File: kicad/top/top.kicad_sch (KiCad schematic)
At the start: 32 parts, among them J1 OLED_128x32, J2 Conn_01x15, SW1 SLW-864574-5A-RA-N-D, SW2 RotaryEncoder_Switch

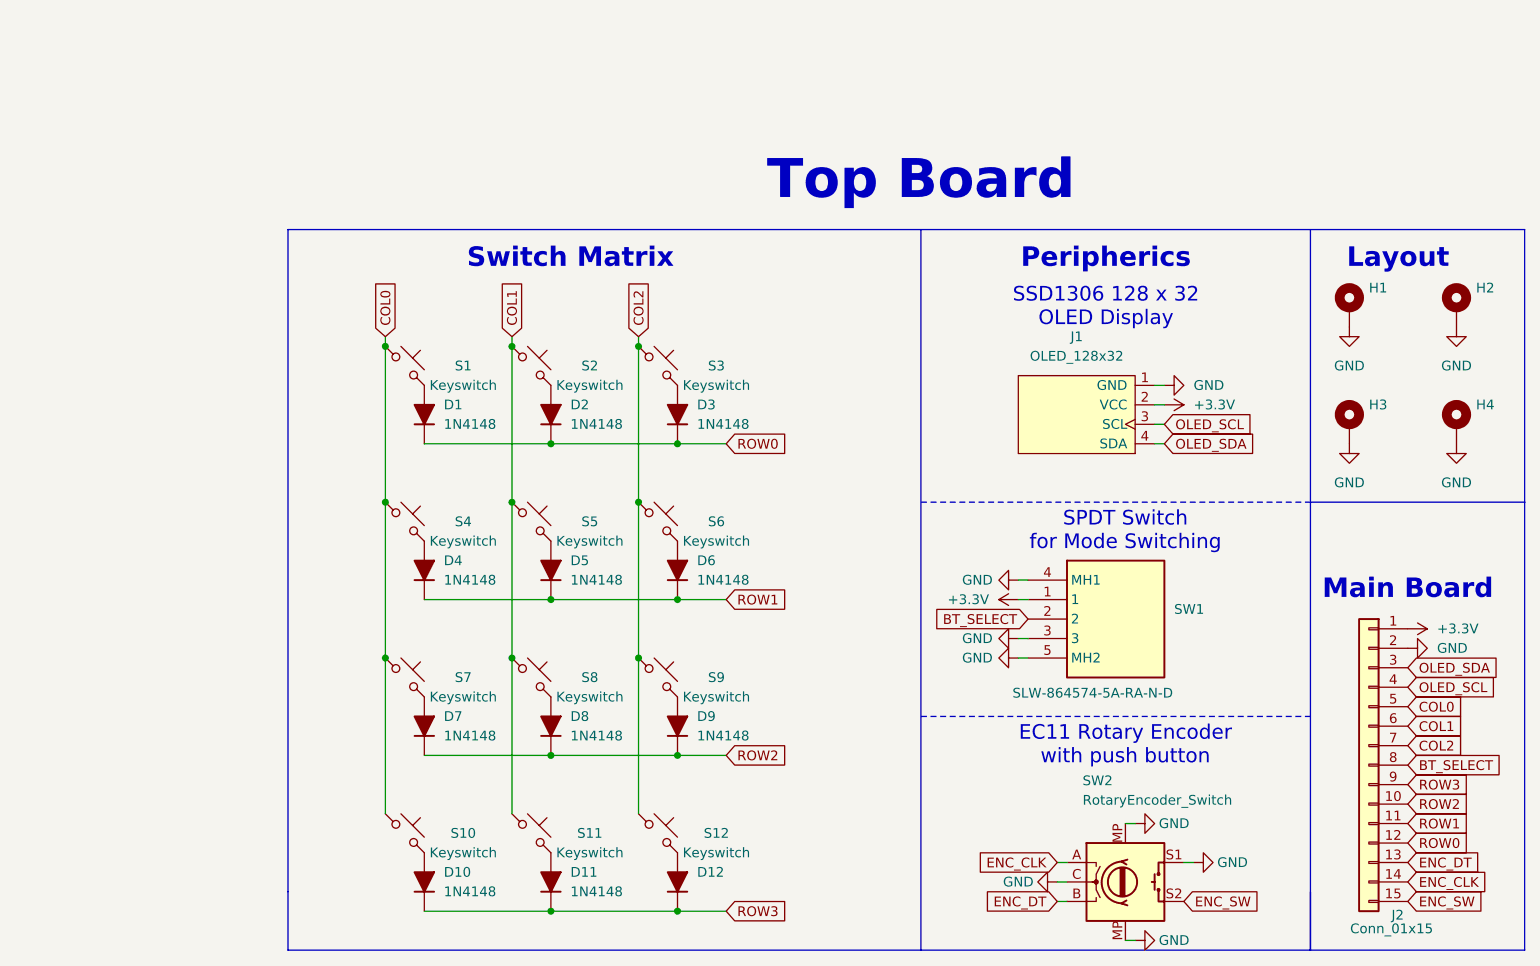
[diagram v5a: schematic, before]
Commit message: added visuals, updated the documentation
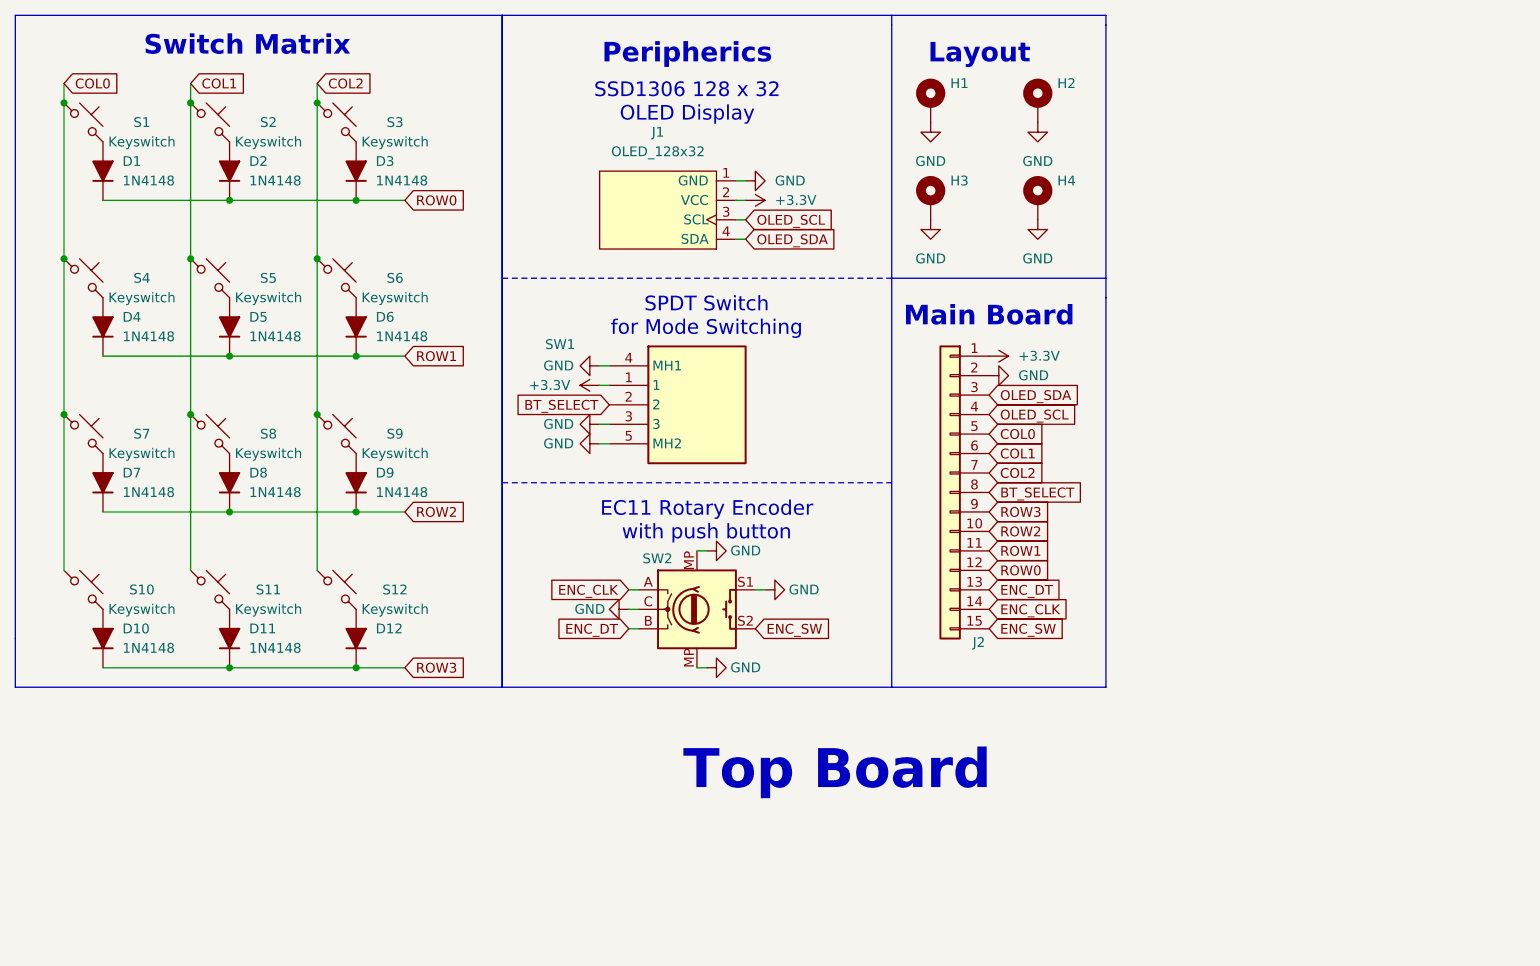
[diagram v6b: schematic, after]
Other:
- moved on the sheet: D1, D10, D11, D12, D2, D3, D4, D5, D6, D7, D8, D9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

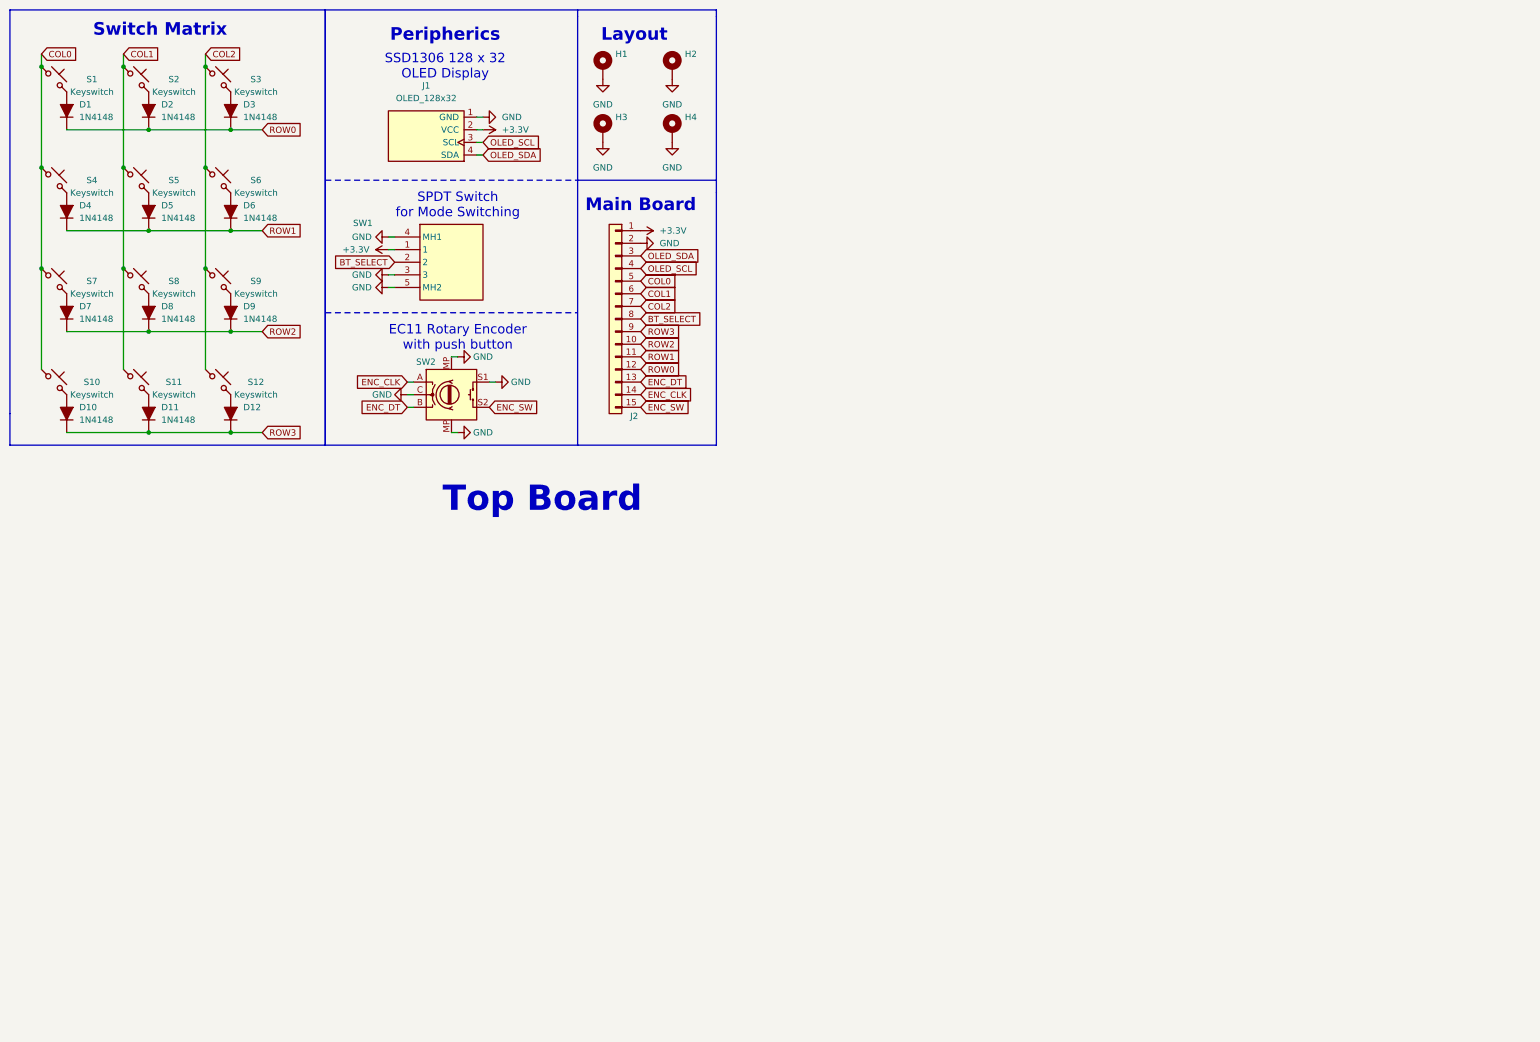
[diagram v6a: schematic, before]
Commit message: update imports, readme, documentatie, add 10 addressable rgbs
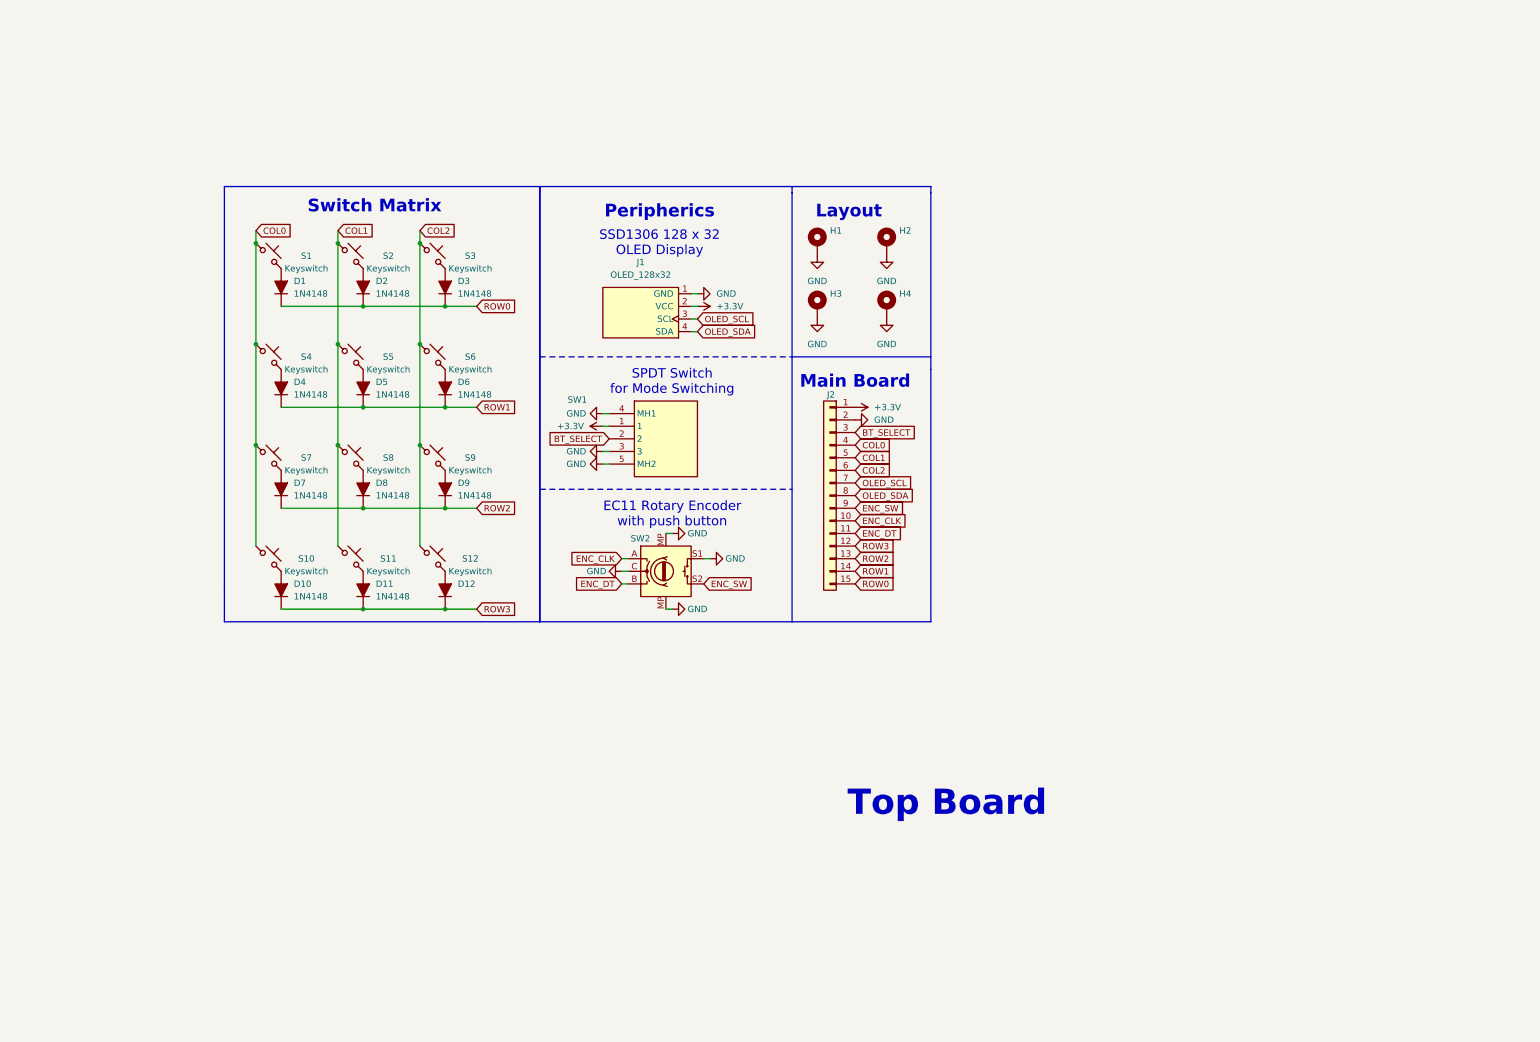
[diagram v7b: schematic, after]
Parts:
- D1, D10, D11, D12, D2, D3, D4, D5, D6, D7, D8, D9: footprint Project-Footprints:D_DO-35_SOD27_P7.62mm_Horizontal -> Top-Footprints:D_DO-35_SOD27_P7.62mm_Horizontal; symbol Top-Library:1N4148 -> Top-Symbols:1N4148
- H1, H2, H3, H4: footprint Project-Footprints:MountingHole_2.2mm_M2_DIN965_Pad -> Top-Footprints:MountingHole_2.2mm_M2_DIN965_Pad; symbol Top-Library:MountingHole_Pad -> Top-Symbols:MountingHole_Pad
- J1: footprint ScottoKeebs_Components:OLED_128x32 -> Top-Footprints:OLED_128x32; symbol ScottoKeebs:OLED_128x32 -> Top-Symbols:OLED_128x32
- J2: footprint Project-Footprints:PinHeader_1x15_P2.54mm_Vertical -> Top-Footprints:PinHeader_1x15_P2.54mm_Vertical; symbol Top-Library:Conn_01x15 -> Top-Symbols:Conn_01x15
- S1, S10, S11, S12, S2, S3, S4, S5, S6, S7, S8, S9: footprint Project-Footprints:MX_Hotswap_1.00u -> Top-Footprints:MX_Hotswap_1.00u; symbol Top-Library:Placeholder_Keyswitch -> Top-Symbols:Placeholder_Keyswitch
- SW1: footprint Project-Footprints:SLW8645745ARAND -> Top-Footprints:SLW8645745ARAND; symbol Top-Library:SLW-864574-5A-RA-N-D -> Top-Symbols:SLW-864574-5A-RA-N-D
- SW2: footprint Project-Footprints:Encoder_EC11_MX -> Top-Footprints:Encoder_EC11_MX; symbol Top-Library:RotaryEncoder_Switch -> Top-Symbols:RotaryEncoder_Switch
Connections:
- net BT_SELECT: now also J2.3 (Pin_3); no longer J2.8 (Pin_8)
- net COL0: now also J2.4 (Pin_4); no longer J2.5 (Pin_5)
- net COL1: now also J2.5 (Pin_5); no longer J2.6 (Pin_6)
- net COL2: now also J2.6 (Pin_6); no longer J2.7 (Pin_7)
- net ENC_CLK: now also J2.10 (Pin_10); no longer J2.14 (Pin_14)
- net ENC_DT: now also J2.11 (Pin_11); no longer J2.13 (Pin_13)
- net ENC_SW: now also J2.9 (Pin_9); no longer J2.15 (Pin_15)
- net OLED_SCL: now also J2.7 (Pin_7); no longer J2.4 (Pin_4)
- net OLED_SDA: now also J2.8 (Pin_8); no longer J2.3 (Pin_3)
- net ROW0: now also J2.15 (Pin_15); no longer J2.12 (Pin_12)
- net ROW1: now also J2.14 (Pin_14); no longer J2.11 (Pin_11)
- net ROW2: now also J2.13 (Pin_13); no longer J2.10 (Pin_10)
- net ROW3: now also J2.12 (Pin_12); no longer J2.9 (Pin_9)
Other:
- moved on the sheet: D1, D10, D11, D12, D2, D3, D4, D5, D6, D7, D8, D9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

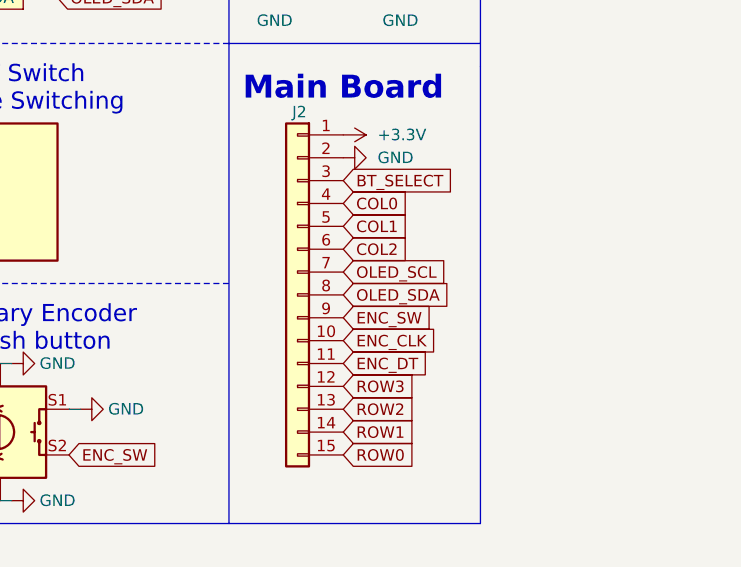
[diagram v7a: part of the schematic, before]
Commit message: Update KiCad project files and documentation
- Adjusted pad dimensions in top.kicad_pro:
  - Drill size changed from 1.0 to 0.8
  - Height changed from 1.7 to 1.6
  - Width changed from 1.7 to 2.0
- Modified design rule for isolated copper from "warning" to "ignore"
- Increased minimum hole clearance from 0.16 to 0.25

- Corrected global label positions for OLED_SDA and OLED_SCL in top.kicad_sch
- Updated footprint properties for mounting holes in top.kicad_sch to "MountingHole:MountingHole_2.5mm_Pad"

- Created new documentation file for component details.
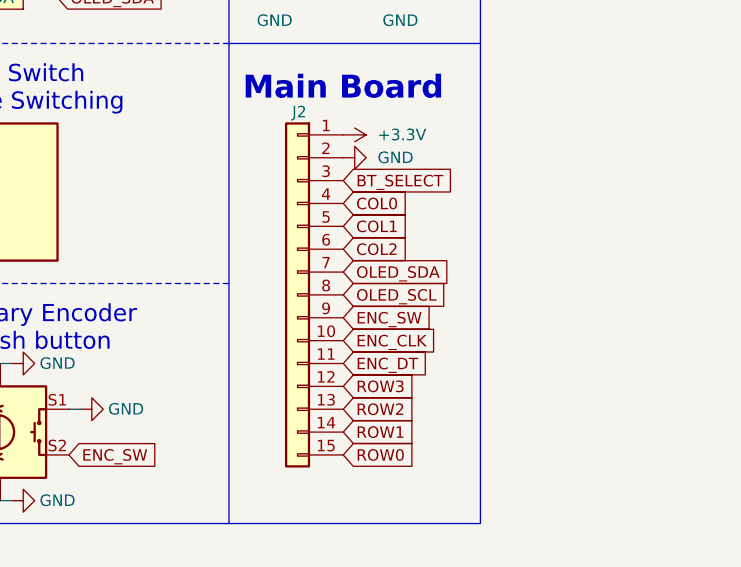
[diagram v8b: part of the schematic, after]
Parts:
- H1, H2, H3, H4: footprint Top-Footprints:MountingHole_2.2mm_M2_DIN965_Pad -> MountingHole:MountingHole_2.5mm_Pad
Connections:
- net OLED_SCL: now also J2.8 (Pin_8); no longer J2.7 (Pin_7)
- net OLED_SDA: now also J2.7 (Pin_7); no longer J2.8 (Pin_8)
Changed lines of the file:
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@@
 	(global_label "OLED_SDA"
 		(shape input)
-		(at 196.85 111.76 0)
+		(at 196.85 109.22 0)
 		(fields_autoplaced yes)
 		(effects
@@
 		)
 		(property "Intersheetrefs" "${INTERSHEET_REFS}"
-			(at 209.1485 111.76 0)
+			(at 209.1485 109.22 0)
 			(effects
 				(font
@@
 	(global_label "OLED_SCL"
 		(shape input)
-		(at 196.85 109.22 0)
+		(at 196.85 111.76 0)
 		(fields_autoplaced yes)
 		(effects
@@
 		)
 		(property "Intersheetrefs" "${INTERSHEET_REFS}"
-			(at 209.088 109.22 0)
+			(at 209.088 111.76 0)
 			(effects
 				(font
@@
 			)
 		)
-		(property "Footprint" "Top-Footprints:MountingHole_2.2mm_M2_DIN965_Pad"
+		(property "Footprint" "MountingHole:MountingHole_2.5mm_Pad"
 			(at 189.23 60.96 0)
 			(effects
@@
 			)
 		)
-		(property "Footprint" "Top-Footprints:MountingHole_2.2mm_M2_DIN965_Pad"
+		(property "Footprint" "MountingHole:MountingHole_2.5mm_Pad"
 			(at 203.2 73.66 0)
 			(effects
@@
 			)
 		)
-		(property "Footprint" "Top-Footprints:MountingHole_2.2mm_M2_DIN965_Pad"
+		(property "Footprint" "MountingHole:MountingHole_2.5mm_Pad"
 			(at 189.23 73.66 0)
 			(effects
@@
 			)
 		)
-		(property "Footprint" "Top-Footprints:MountingHole_2.2mm_M2_DIN965_Pad"
+		(property "Footprint" "MountingHole:MountingHole_2.5mm_Pad"
 			(at 203.2 60.96 0)
 			(effects
